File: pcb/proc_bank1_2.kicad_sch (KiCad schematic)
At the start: 1 part

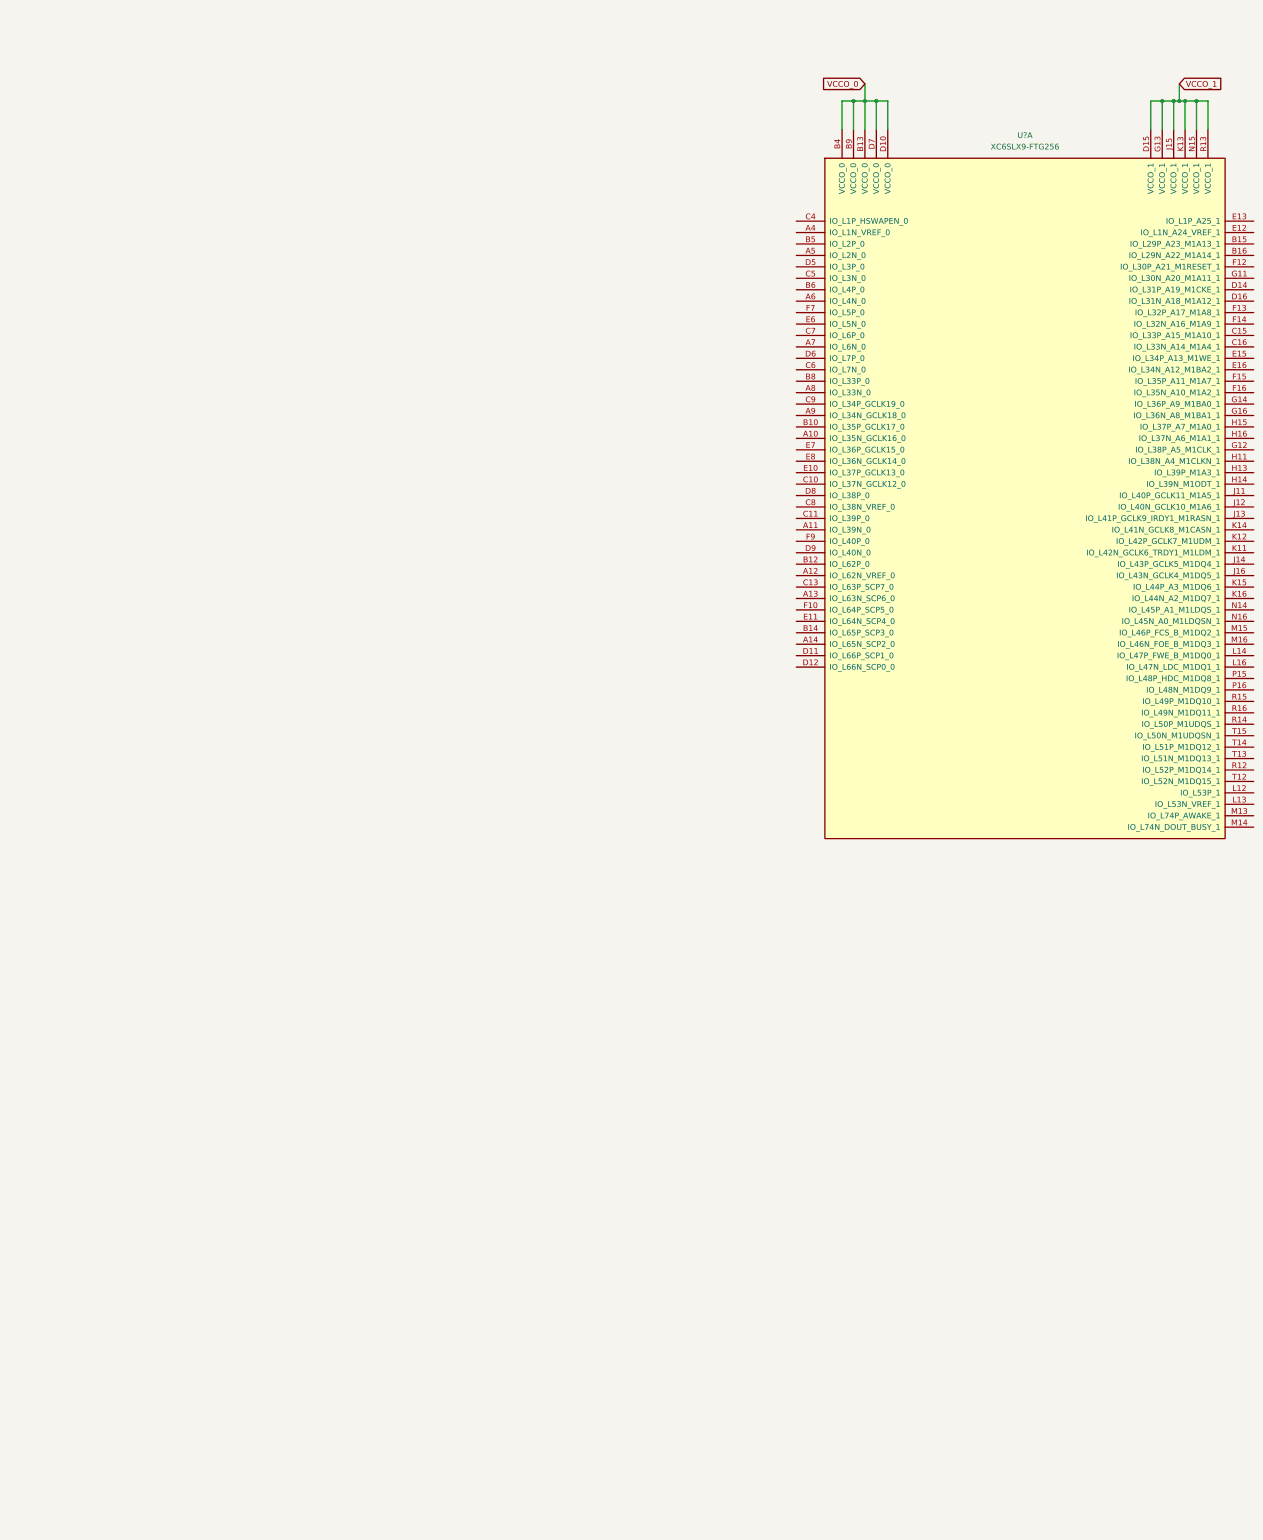
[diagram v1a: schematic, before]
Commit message: add the din connector
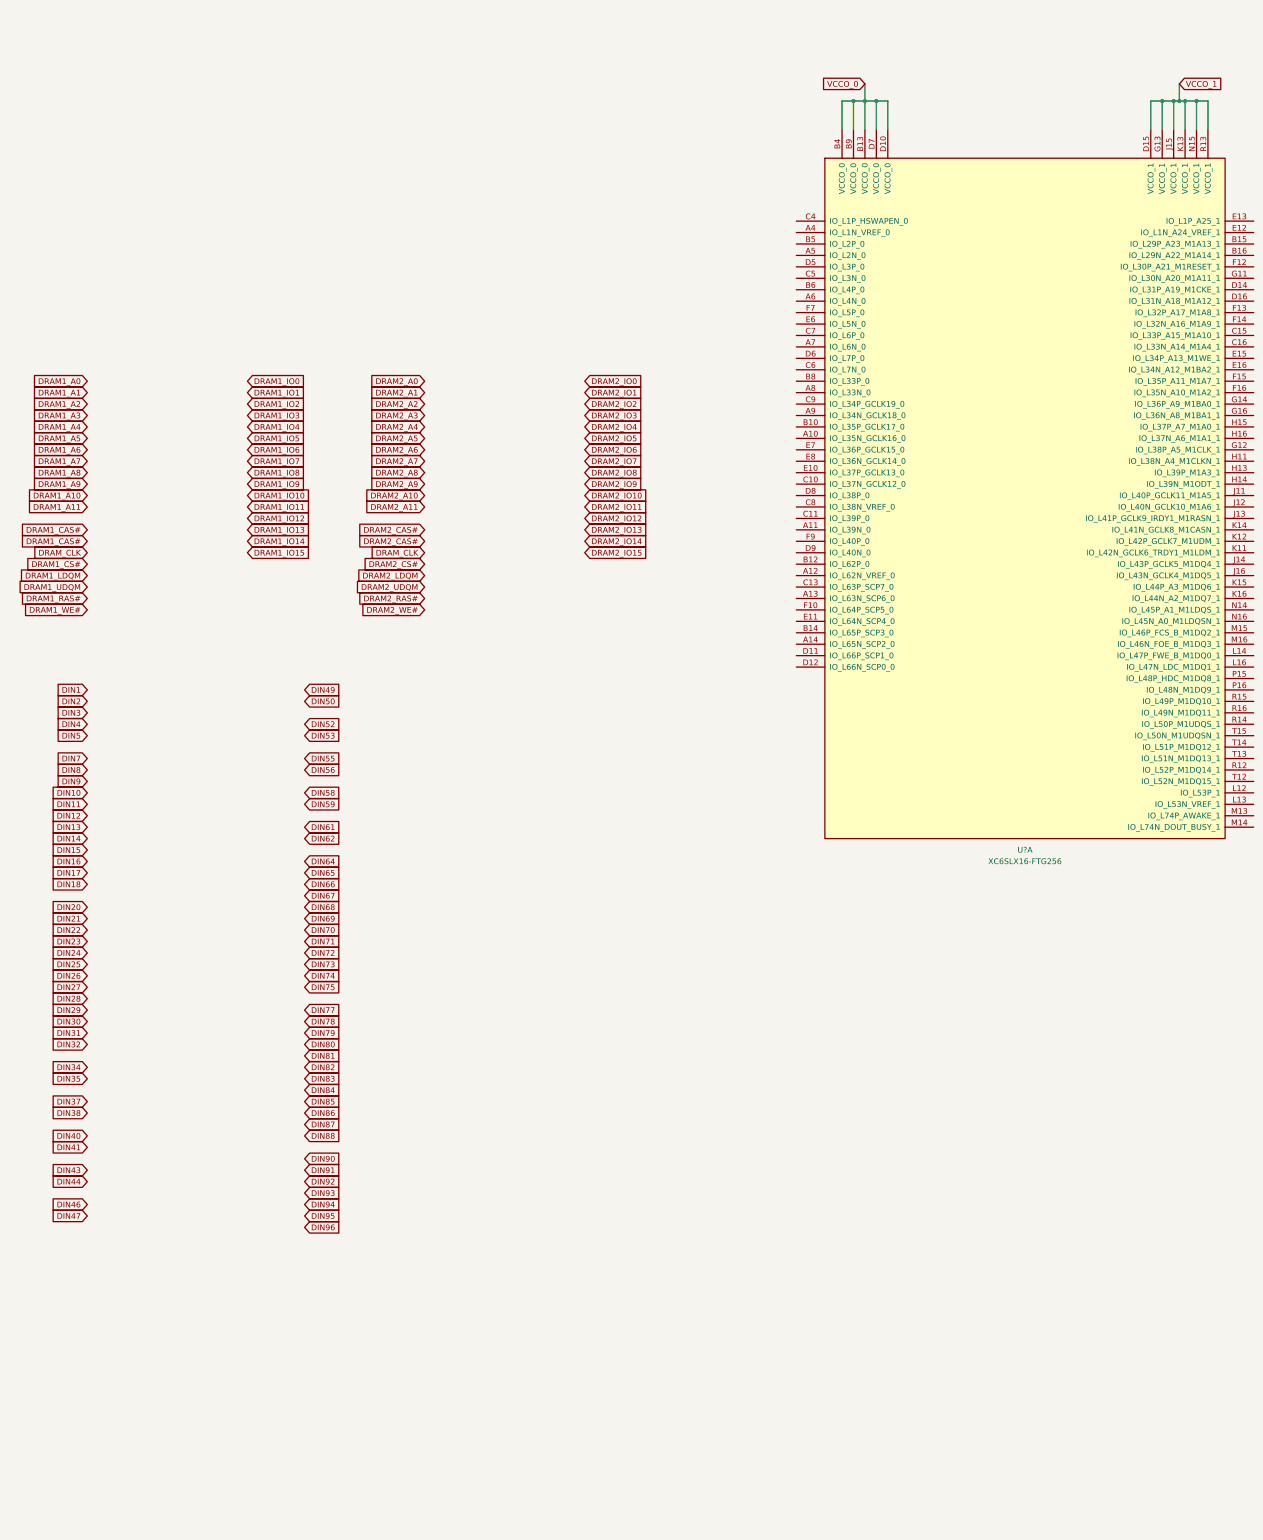
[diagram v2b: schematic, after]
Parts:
- removed U?: XC6SLX9-FTG256, symbol FPGA_Xilinx_Spartan6:XC6SLX9-FTG256
- added U?: XC6SLX16-FTG256, symbol FPGA_Xilinx_Spartan6:XC6SLX16-FTG256
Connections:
- net VCCO_0: now also U?.B13 (VCCO_0), U?.B4 (VCCO_0), U?.B9 (VCCO_0), U?.D10 (VCCO_0), U?.D7 (VCCO_0)
- net VCCO_1: now also U?.D15 (VCCO_1), U?.G13 (VCCO_1), U?.J15 (VCCO_1), U?.K13 (VCCO_1), U?.N15 (VCCO_1), U?.R13 (VCCO_1)

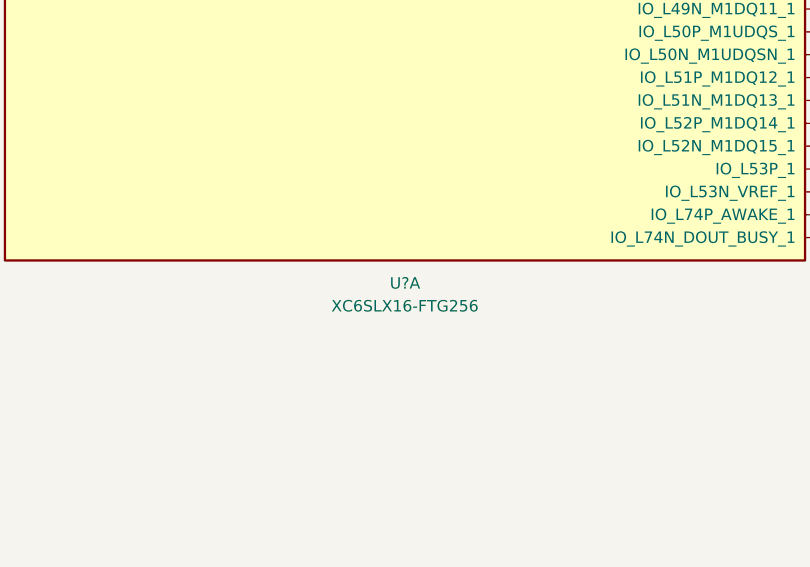
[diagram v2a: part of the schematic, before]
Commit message: start associating footprints
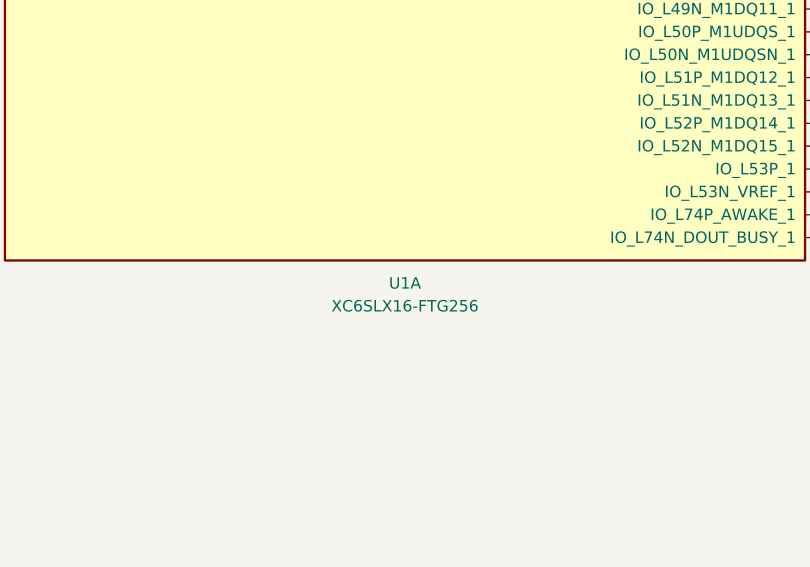
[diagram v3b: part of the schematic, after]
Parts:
- gave numbers to parts that had none: 1
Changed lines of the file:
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@@
   (symbol (lib_id "FPGA_Xilinx_Spartan6:XC6SLX16-FTG256") (at 161.29 133.35 0) (unit 1)
     (in_bom yes) (on_board yes) (fields_autoplaced)
-    (property "Reference" "U?" (id 0) (at 161.29 214.63 0))
+    (property "Reference" "U1" (id 0) (at 161.29 214.63 0))
     (property "Value" "XC6SLX16-FTG256" (id 1) (at 161.29 217.17 0))
     (property "Footprint" "" (id 2) (at 161.29 133.35 0)

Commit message: add tps541620 footprint
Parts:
- added C90: 100uF, Capacitor_SMD:C_1210_3225Metric, symbol Device:C_Small
- added U14: ECS-7050MV, Oscillator:ECS-7050MV, symbol Oscillator:ECS-7050MV
- U1: footprint (none) -> Package_BGA:Xilinx_FTG256
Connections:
- new net +3V3: C90.1, U14.4 (VDD)
- new net GND: C90.2, U14.2 (GND)
- no-connect marks 0 -> 1
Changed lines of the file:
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@@
 (kicad_sch (version 20210126) (generator eeschema)
   (paper "User" 319.989 280.01)
+  (junction (at 35.56 220.98) (diameter 0.9144) (color 0 0 0 0))
   (junction (at 123.19 48.26) (diameter 0.9144) (color 0 0 0 0))
   (junction (at 125.73 48.26) (diameter 0.9144) (color 0 0 0 0))
@@
   (junction (at 196.85 48.26) (diameter 0.9144) (color 0 0 0 0))
   (junction (at 199.39 48.26) (diameter 0.9144) (color 0 0 0 0))
+  (no_connect (at 62.23 227.33))
+  (wire (pts (xy 35.56 218.44) (xy 35.56 220.98))
+    (stroke (width 0) (type solid) (color 0 0 0 0))
+  )
+  (wire (pts (xy 35.56 220.98) (xy 45.72 220.98))
+    (stroke (width 0) (type solid) (color 0 0 0 0))
+  )
+  (wire (pts (xy 35.56 223.52) (xy 35.56 220.98))
+    (stroke (width 0) (type solid) (color 0 0 0 0))
+  )
+  (wire (pts (xy 35.56 228.6) (xy 35.56 233.68))
+    (stroke (width 0) (type solid) (color 0 0 0 0))
+  )
+  (wire (pts (xy 72.39 215.9) (xy 72.39 218.44))
+    (stroke (width 0) (type solid) (color 0 0 0 0))
+  )
+  (wire (pts (xy 72.39 236.22) (xy 72.39 238.76))
+    (stroke (width 0) (type solid) (color 0 0 0 0))
+  )
   (wire (pts (xy 120.65 48.26) (xy 123.19 48.26))
     (stroke (width 0) (type solid) (color 0 0 0 0))
@@
     (stroke (width 0) (type solid) (color 0 0 0 0))
   )
+  (label "CLK_VCC" (at 45.72 220.98 0)
+    (effects (font (size 1.27 1.27)) (justify left bottom))
+  )
+  (label "CLK_VCC" (at 72.39 215.9 180)
+    (effects (font (size 1.27 1.27)) (justify right bottom))
+  )
   (global_label "DRAM1_A0" (shape input) (at -46.99 110.49 180) (fields_autoplaced)
     (effects (font (size 1.27 1.27)) (justify right))
@@
       (effects (font (size 1.27 1.27)) (justify left) hide)
     )
+  )
+  (symbol (lib_id "power:+3V3") (at 35.56 218.44 0) (unit 1)
+    (in_bom yes) (on_board yes) (fields_autoplaced)
+    (property "Reference" "#PWR0105" (id 0) (at 35.56 222.25 0)
+      (effects (font (size 1.27 1.27)) hide)
+    )
+    (property "Value" "+3V3" (id 1) (at 35.56 214.63 0))
+    (property "Footprint" "" (id 2) (at 35.56 218.44 0)
+      (effects (font (size 1.27 1.27)) hide)
+    )
+    (property "Datasheet" "" (id 3) (at 35.56 218.44 0)
+      (effects (font (size 1.27 1.27)) hide)
+    )
+    (pin "1")
+  )
+  (symbol (lib_id "power:GND") (at 35.56 233.68 0) (unit 1)
+    (in_bom yes) (on_board yes) (fields_autoplaced)
+    (property "Reference" "#PWR0106" (id 0) (at 35.56 240.03 0)
+      (effects (font (size 1.27 1.27)) hide)
+    )
+    (property "Value" "GND" (id 1) (at 35.56 238.76 0))
+    (property "Footprint" "" (id 2) (at 35.56 233.68 0)
+      (effects (font (size 1.27 1.27)) hide)
+    )
+    (property "Datasheet" "" (id 3) (at 35.56 233.68 0)
+      (effects (font (size 1.27 1.27)) hide)
+    )
+    (pin "1")
+  )
+  (symbol (lib_id "power:GND") (at 72.39 238.76 0) (unit 1)
+    (in_bom yes) (on_board yes) (fields_autoplaced)
+    (property "Reference" "#PWR0104" (id 0) (at 72.39 245.11 0)
+      (effects (font (size 1.27 1.27)) hide)
+    )
+    (property "Value" "GND" (id 1) (at 72.39 243.84 0))
+    (property "Footprint" "" (id 2) (at 72.39 238.76 0)
+      (effects (font (size 1.27 1.27)) hide)
+    )
+    (property "Datasheet" "" (id 3) (at 72.39 238.76 0)
+      (effects (font (size 1.27 1.27)) hide)
+    )
+    (pin "1")
+  )
+  (symbol (lib_id "Device:C_Small") (at 35.56 226.06 0) (unit 1)
+    (in_bom yes) (on_board yes)
+    (property "Reference" "C90" (id 0) (at 38.1 225.4249 0)
+      (effects (font (size 1.27 1.27)) (justify left))
+    )
+    (property "Value" "100uF" (id 1) (at 38.1 227.9649 0)
+      (effects (font (size 1.27 1.27)) (justify left))
+    )
+    (property "Footprint" "Capacitor_SMD:C_1210_3225Metric" (id 2) (at 35.56 226.06 0)
+      (effects (font (size 1.27 1.27)) hide)
+    )
+    (property "Datasheet" "~" (id 3) (at 35.56 226.06 0)
+      (effects (font (size 1.27 1.27)) hide)
+    )
+    (pin "1")
+    (pin "2")
+  )
+  (symbol (lib_id "Oscillator:ECS-7050MV") (at 72.39 227.33 0) (unit 1)
+    (in_bom yes) (on_board yes)
+    (property "Reference" "U14" (id 0) (at 78.74 217.8049 0)
+      (effects (font (size 1.27 1.27)) (justify left))
+    )
+    (property "Value" "ECS-7050MV" (id 1) (at 74.93 220.3449 0)
+      (effects (font (size 1.27 1.27)) (justify left))
+    )
+    (property "Footprint" "Oscillator:ECS-7050MV" (id 2) (at 64.77 219.71 0)
+      (effects (font (size 1.27 1.27)) hide)
+    )
+    (property "Datasheet" "" (id 3) (at 64.77 219.71 0)
+      (effects (font (size 1.27 1.27)) hide)
+    )
+    (pin "1")
+    (pin "2")
+    (pin "3")
+    (pin "4")
   )
   (symbol (lib_id "FPGA_Xilinx_Spartan6:XC6SLX16-FTG256") (at 161.29 133.35 0) (unit 1)
@@
     (property "Reference" "U1" (id 0) (at 161.29 214.63 0))
     (property "Value" "XC6SLX16-FTG256" (id 1) (at 161.29 217.17 0))
-    (property "Footprint" "" (id 2) (at 161.29 133.35 0)
-      (effects (font (size 1.27 1.27)) hide)
-    )
+    (property "Footprint" "Package_BGA:Xilinx_FTG256" (id 2) (at 161.29 133.35 0)
+      (effects (font (size 1.27 1.27)) hide)
+    )

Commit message: add components to pcb
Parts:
- U14: footprint Oscillator:ECS-7050MV -> ECS-7050MV:ECS-7050MV
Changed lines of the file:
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@@
-(kicad_sch (version 20210126) (generator eeschema)
+(kicad_sch (version 20210406) (generator eeschema)
   (paper "User" 319.989 280.01)
   (junction (at 35.56 220.98) (diameter 0.9144) (color 0 0 0 0))
@@
       (effects (font (size 1.27 1.27)) (justify left))
     )
-    (property "Footprint" "Oscillator:ECS-7050MV" (id 2) (at 64.77 219.71 0)
+    (property "Footprint" "ECS-7050MV:ECS-7050MV" (id 2) (at 64.77 219.71 0)
       (effects (font (size 1.27 1.27)) hide)
     )
